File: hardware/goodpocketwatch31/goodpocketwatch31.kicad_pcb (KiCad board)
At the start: 2 copper layers, 75.2 x 101.2 mm, 56 parts, among them J1 ANT_U.FL, J2 DX07S016JA1R1500, J3 SMA, SW0 SW_Push, SW1 SW_Push, SW10 SW_Push, SW11 SW_Push, SW12 SW_Push, SW13 SW_Push, SW14 SW_Push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

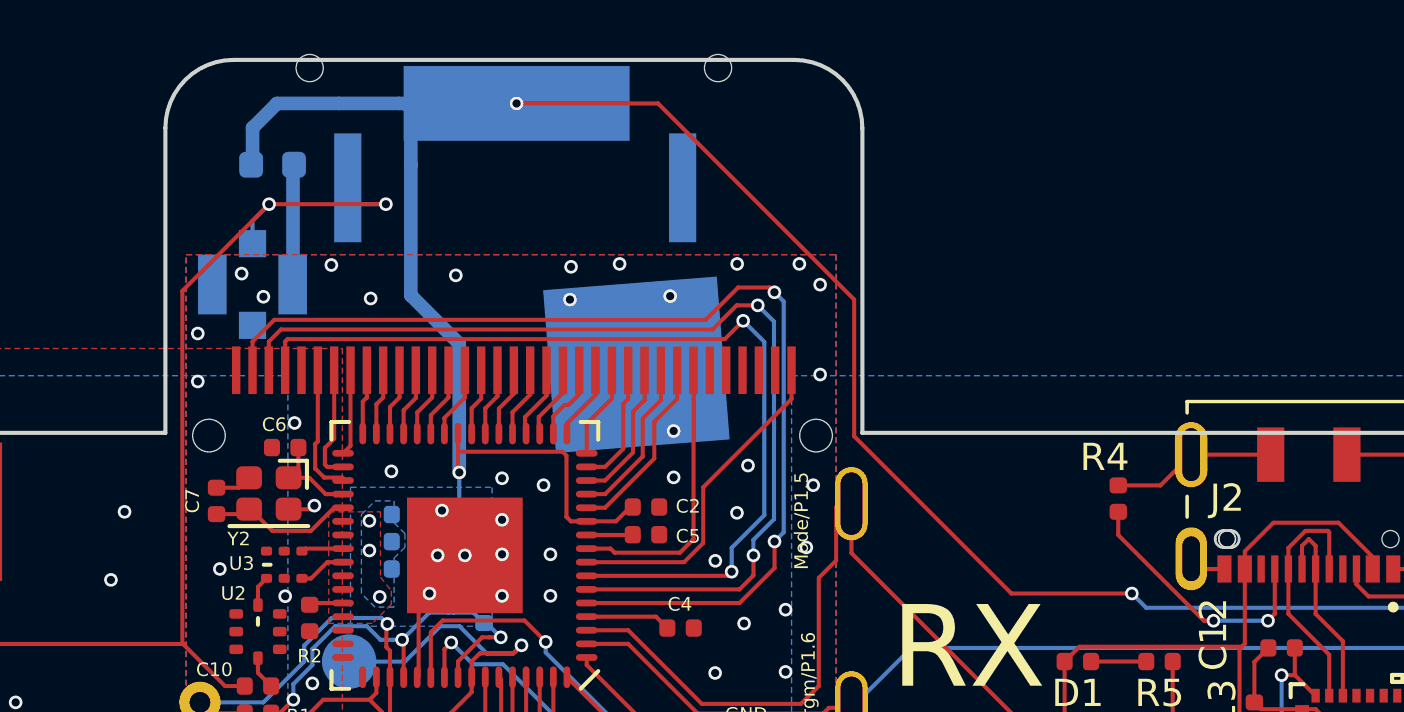
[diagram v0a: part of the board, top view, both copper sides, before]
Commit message: Conversion of GoodPocketWatch31 to Kicad6. #147
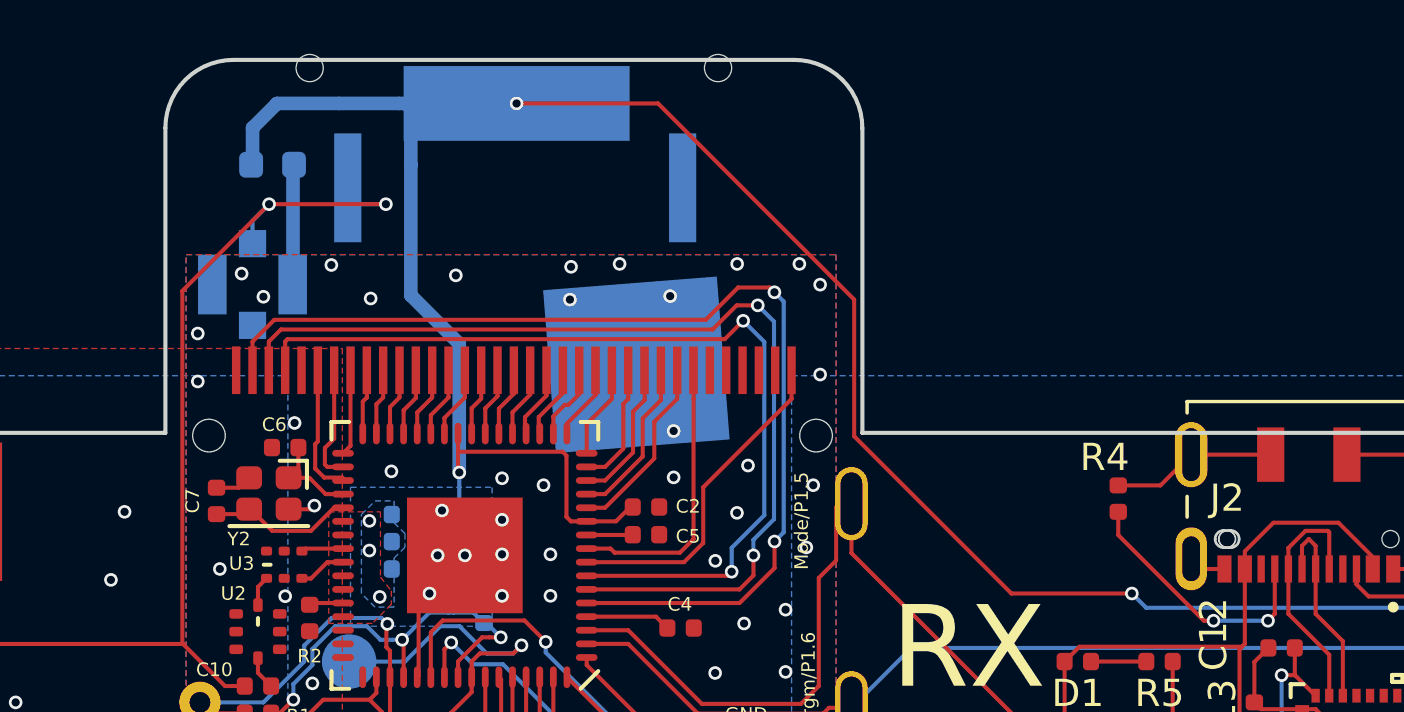
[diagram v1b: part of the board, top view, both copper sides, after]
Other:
- net class Default removed
